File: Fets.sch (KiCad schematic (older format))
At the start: 9 parts, among them Q1 SEMiX402GB066HDs, Q2 SEMiX402GB066HDs, Q3 SEMiX402GB066HDs

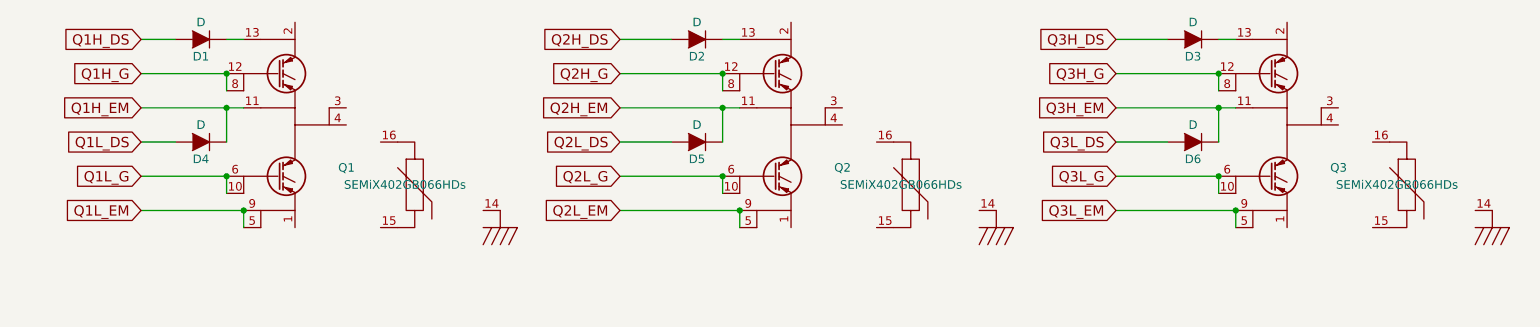
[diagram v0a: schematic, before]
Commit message: added gate drivers, increased FET spacing
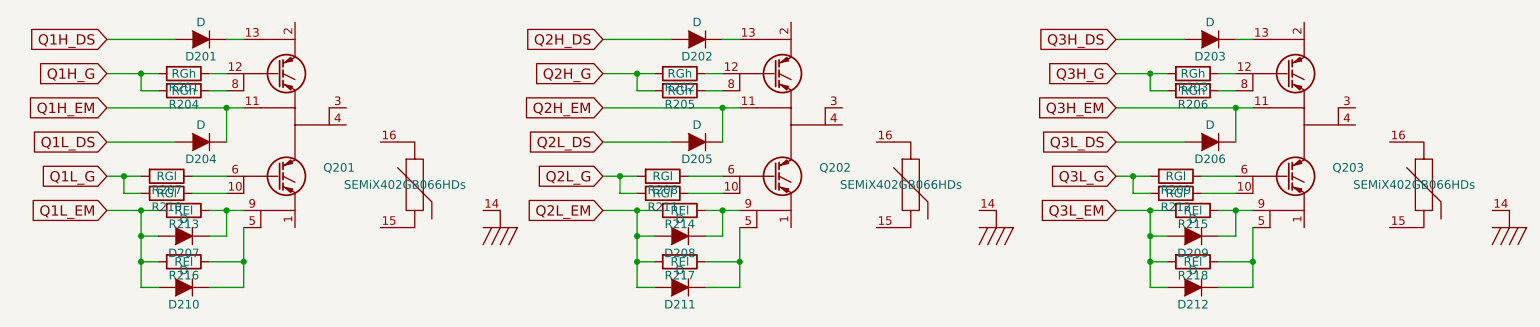
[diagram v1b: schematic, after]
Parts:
- removed D2, D3, D5, D6: D, Diodes_SMD:MELF_Standard, symbol D
- added D202, D203, D205, D206: D, Diodes_SMD:MELF_Standard, symbol D
- added D207, D208, D209, D210, D211, D212: D, Diodes_SMD:DO-214AB, symbol D
- added R201, R202, R203, R204, R205, R206: RGh, Resistors_SMD:R_1812, symbol R
- added R207, R208, R209, R210, R211, R212: RGl, Resistors_SMD:R_1812, symbol R
- added R213, R214, R215, R216, R217, R218: REl, Resistors_SMD:R_1812, symbol R
- Q201: renamed from Q1; footprint VFD_parts:SEMiX_2s -> VFD_parts:SEMiX_2s_7nc
- Q202: renamed from Q2; footprint VFD_parts:SEMiX_2s -> VFD_parts:SEMiX_2s_7nc
- Q203: renamed from Q3; footprint VFD_parts:SEMiX_2s -> VFD_parts:SEMiX_2s_7nc
- renumbered D1 to D201, D4 to D204
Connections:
- net Q1H_G: now also R201.2, R204.2; no longer Q201.12, Q201.8
- net Q1L_EM: now also D207.2 (A), D210.2 (A), R213.2, R216.2; no longer Q201.5, Q201.9
- net Q1L_G: now also R207.2, R210.2; no longer Q201.10, Q201.6
- net Q2H_DS: now also D202.2 (A)
- net Q2H_EM: now also D205.1 (K)
- net Q2H_G: now also R202.2, R205.2; no longer Q202.12, Q202.8
- net Q2L_DS: now also D205.2 (A)
- net Q2L_EM: now also D208.2 (A), D211.2 (A), R214.2, R217.2; no longer Q202.5, Q202.9
- net Q2L_G: now also R208.2, R211.2; no longer Q202.10, Q202.6
- net Q3H_DS: now also D203.2 (A)
- net Q3H_EM: now also D206.1 (K)
- net Q3H_G: now also R203.2, R206.2; no longer Q203.12, Q203.8
- net Q3L_DS: now also D206.2 (A)
- net Q3L_EM: now also D209.2 (A), D212.2 (A), R215.2, R218.2; no longer Q203.5, Q203.9
- net Q3L_G: now also R209.2, R212.2; no longer Q203.10, Q203.6
- net at Q202.13: now also D202.1 (K)
- net at Q203.13: now also D203.1 (K)
- new net: Q201.10, R210.1
- new net: Q201.12, R201.1
- new net: D210.1 (K), Q201.5, R216.1
- new net: Q201.6, R207.1
- new net: Q201.8, R204.1
- new net: D207.1 (K), Q201.9, R213.1
- new net: Q202.10, R211.1
- new net: Q202.12, R202.1
- new net: D211.1 (K), Q202.5, R217.1
- new net: Q202.6, R208.1
- new net: Q202.8, R205.1
- new net: D208.1 (K), Q202.9, R214.1
- new net: Q203.10, R212.1
- new net: Q203.12, R203.1
- new net: D212.1 (K), Q203.5, R218.1
- new net: Q203.6, R209.1
- new net: Q203.8, R206.1
- new net: D209.1 (K), Q203.9, R215.1
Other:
- moved on the sheet: Q203
